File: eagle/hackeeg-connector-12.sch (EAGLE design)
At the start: 21 parts

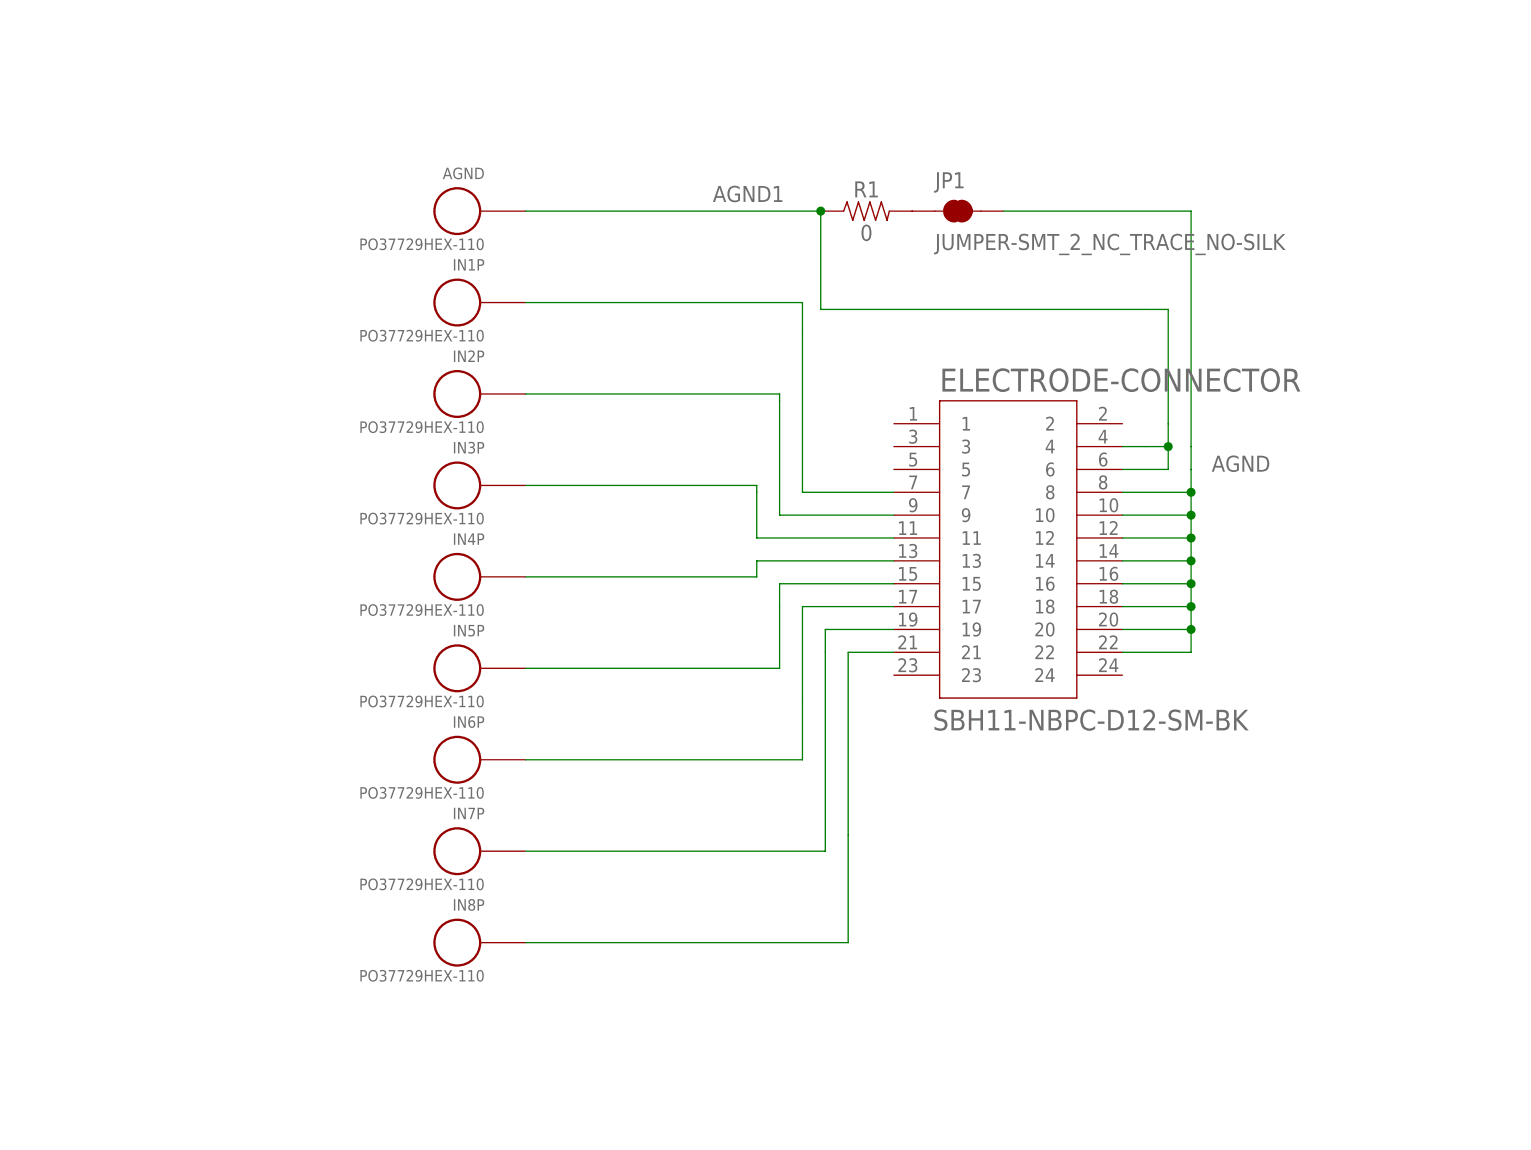
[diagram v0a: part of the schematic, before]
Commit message: added connector, finished schematic and routed
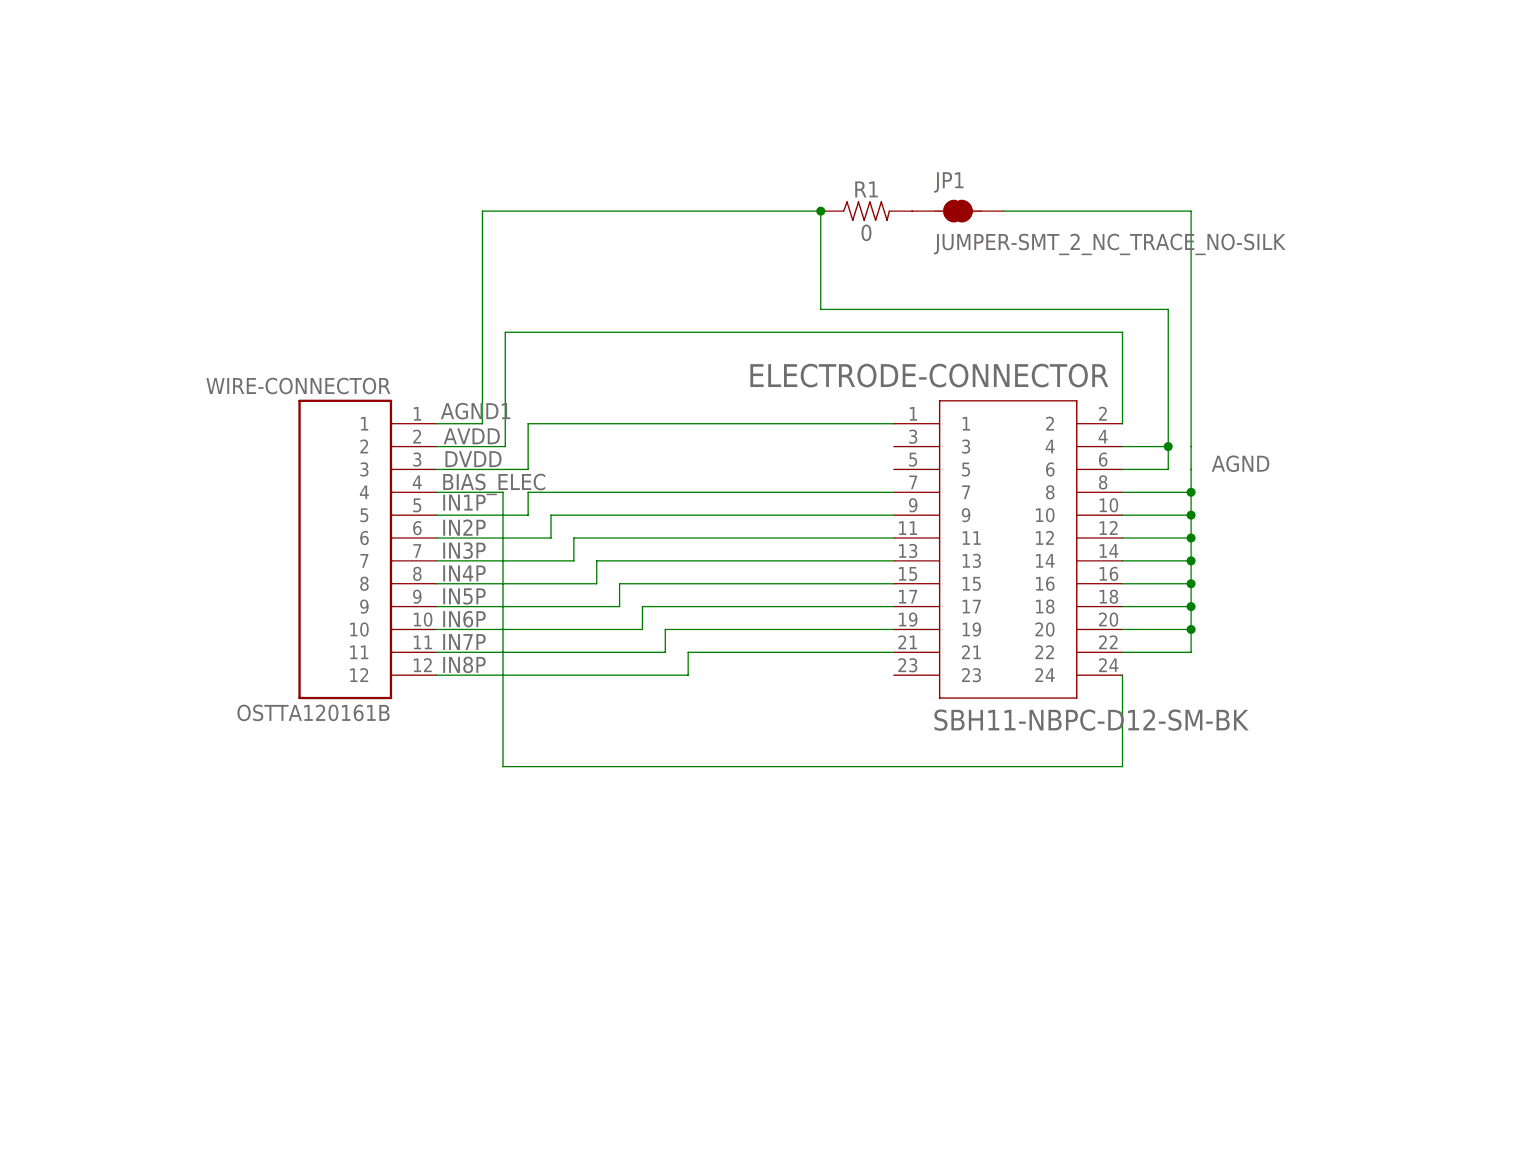
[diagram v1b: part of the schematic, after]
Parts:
- removed AGND, IN1P, IN2P, IN3P, IN4P, IN5P, IN6P, IN7P, IN8P: PO37729HEX-110, po-37729:PO37729HEX-110
- added WIRE-CONNECTOR: OSTTA120161B, OSTTA120161B:OSTTA120161B
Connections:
- removed net N$2: ELECTRODE-CONNECTOR.7, IN1P.SIGNAL
- removed net N$3: ELECTRODE-CONNECTOR.9, IN2P.SIGNAL
- removed net N$4: ELECTRODE-CONNECTOR.11, IN3P.SIGNAL
- removed net N$5: ELECTRODE-CONNECTOR.13, IN4P.SIGNAL
- removed net N$6: ELECTRODE-CONNECTOR.15, IN5P.SIGNAL
- removed net N$7: ELECTRODE-CONNECTOR.17, IN6P.SIGNAL
- removed net N$8: ELECTRODE-CONNECTOR.19, IN7P.SIGNAL
- removed net N$9: ELECTRODE-CONNECTOR.21, IN8P.SIGNAL
- new net AVDD: ELECTRODE-CONNECTOR.2, WIRE-CONNECTOR.2
- new net BIAS_ELEC: ELECTRODE-CONNECTOR.24, WIRE-CONNECTOR.4
- new net DVDD: ELECTRODE-CONNECTOR.1, WIRE-CONNECTOR.3
- new net IN1P: ELECTRODE-CONNECTOR.7, WIRE-CONNECTOR.5
- new net IN2P: ELECTRODE-CONNECTOR.9, WIRE-CONNECTOR.6
- new net IN3P: ELECTRODE-CONNECTOR.11, WIRE-CONNECTOR.7
- new net IN4P: ELECTRODE-CONNECTOR.13, WIRE-CONNECTOR.8
- new net IN5P: ELECTRODE-CONNECTOR.15, WIRE-CONNECTOR.9
- new net IN6P: ELECTRODE-CONNECTOR.17, WIRE-CONNECTOR.10
- new net IN7P: ELECTRODE-CONNECTOR.19, WIRE-CONNECTOR.11
- new net IN8P: ELECTRODE-CONNECTOR.21, WIRE-CONNECTOR.12
- net AGND1: now also WIRE-CONNECTOR.1; no longer AGND.SIGNAL

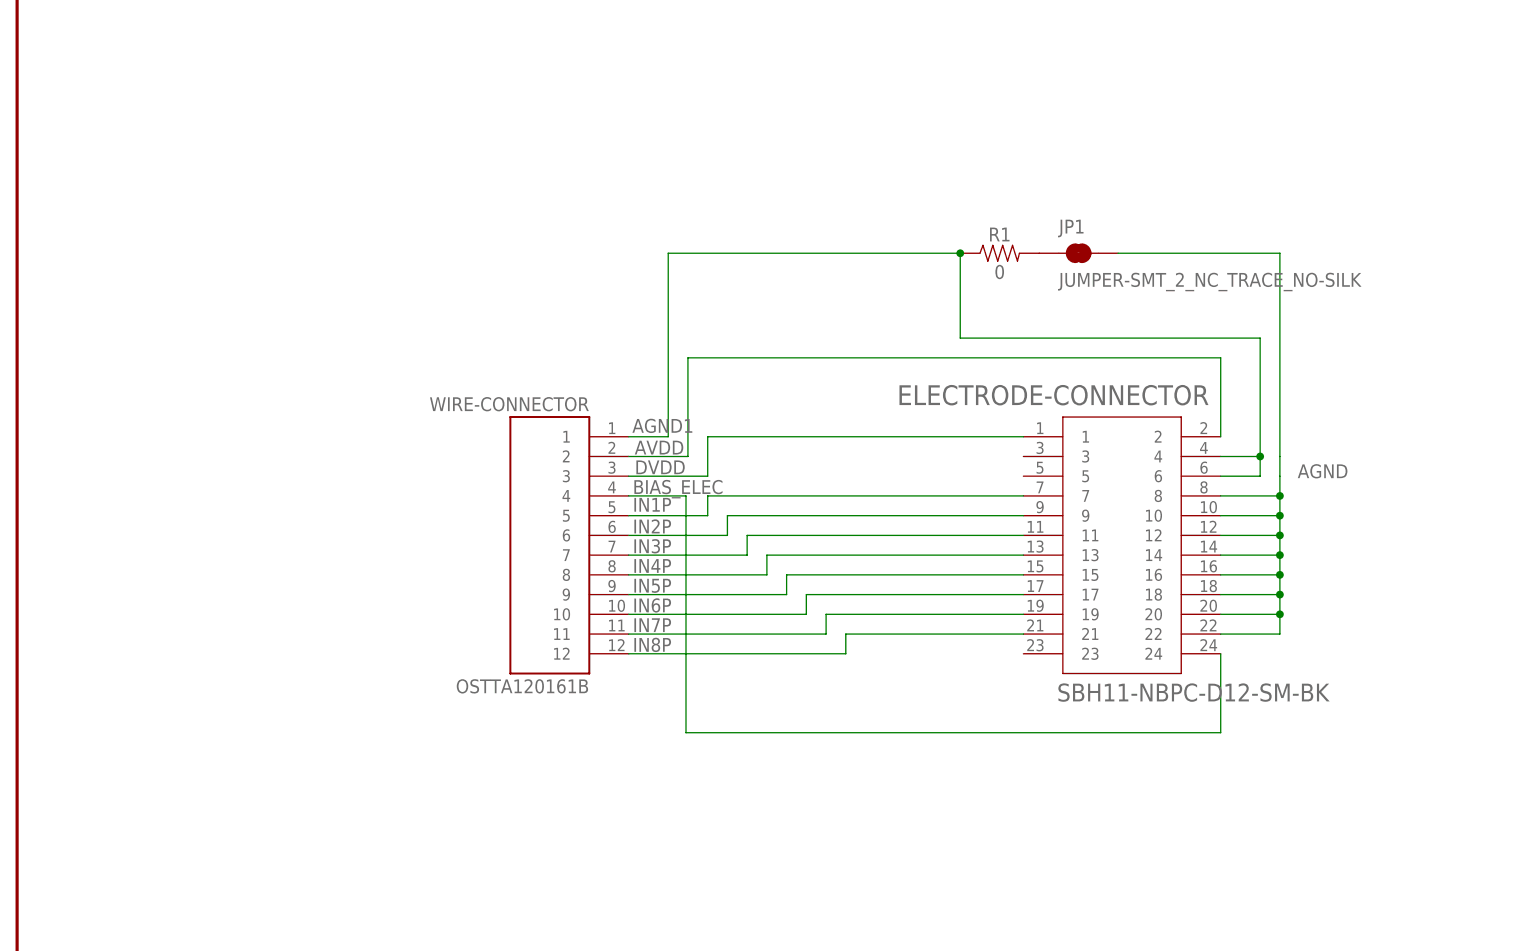
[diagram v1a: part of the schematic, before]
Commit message: put wire connector on bottom of board
- labeled wire connector pins
- board is routed
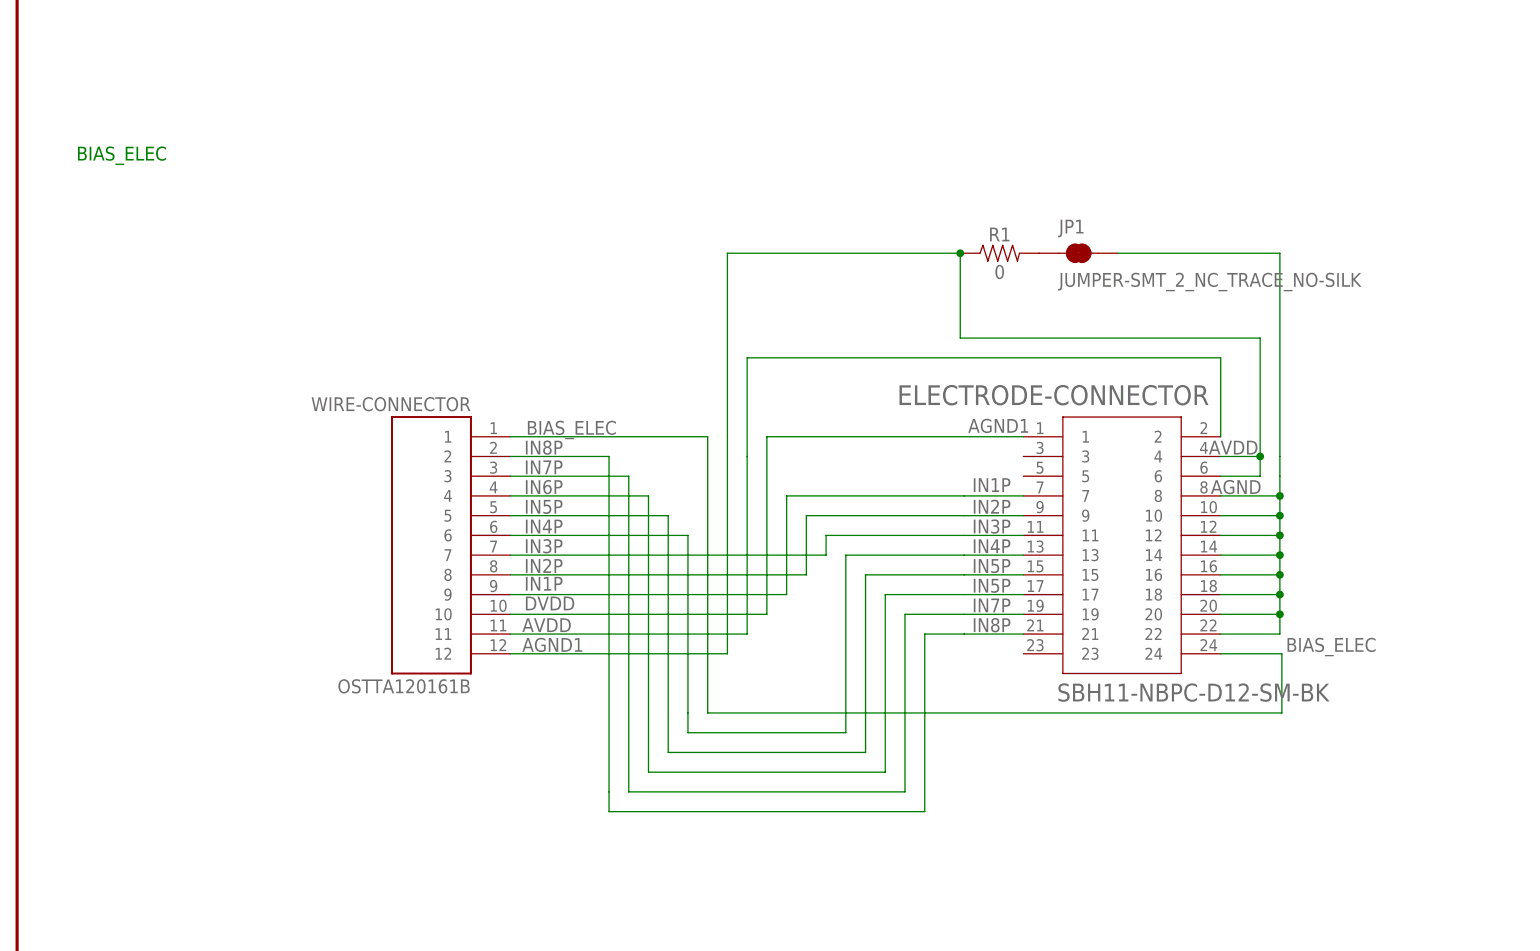
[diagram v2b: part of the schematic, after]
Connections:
- net AGND1: now also WIRE-CONNECTOR.12; no longer WIRE-CONNECTOR.1
- net AVDD: now also WIRE-CONNECTOR.11; no longer WIRE-CONNECTOR.2
- net BIAS_ELEC: now also WIRE-CONNECTOR.1; no longer WIRE-CONNECTOR.4
- net DVDD: now also WIRE-CONNECTOR.10; no longer WIRE-CONNECTOR.3
- net IN1P: now also WIRE-CONNECTOR.9; no longer WIRE-CONNECTOR.5
- net IN2P: now also WIRE-CONNECTOR.8; no longer WIRE-CONNECTOR.6
- net IN4P: now also WIRE-CONNECTOR.6; no longer WIRE-CONNECTOR.8
- net IN5P: now also WIRE-CONNECTOR.5; no longer WIRE-CONNECTOR.9
- net IN6P: now also WIRE-CONNECTOR.4; no longer WIRE-CONNECTOR.10
- net IN7P: now also WIRE-CONNECTOR.3; no longer WIRE-CONNECTOR.11
- net IN8P: now also WIRE-CONNECTOR.2; no longer WIRE-CONNECTOR.12
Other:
- note added: "AGND1"
- note added: "AVDD"
- note added: "BIAS_ELEC"
- note added: "IN1P"
- note added: "IN2P"
- note added: "IN3P"
- note added: "IN4P"
- note added: "IN5P"
- note added: "IN7P"
- note added: "IN8P"
- moved on the sheet: WIRE-CONNECTOR

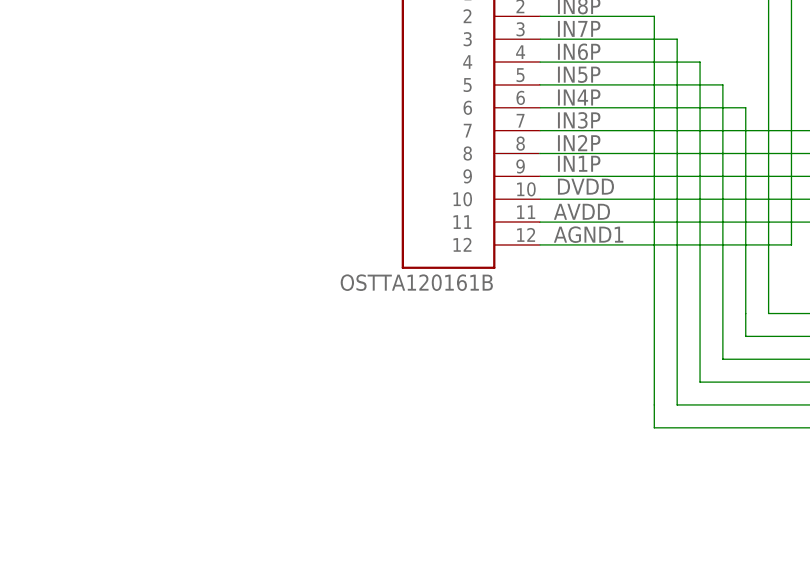
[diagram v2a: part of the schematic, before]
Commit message: replaced OSTTA120161B with OSTTA120161 library
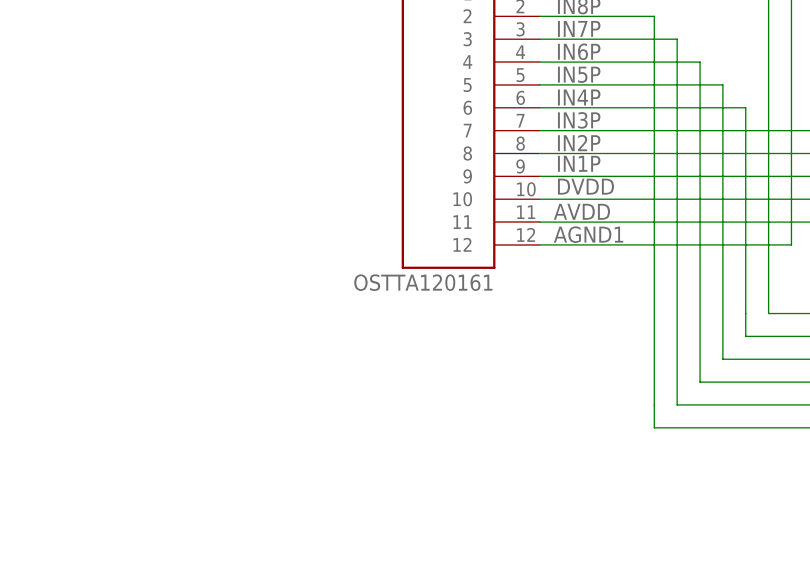
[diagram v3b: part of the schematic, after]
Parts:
- WIRE-CONNECTOR: value OSTTA120161B -> OSTTA120161; device OSTTA120161B:OSTTA120161B -> OSTTA120161:OSTTA120161
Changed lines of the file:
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@@
 <part name="R1" library="SparkFun-Resistors" library_urn="urn:adsk.eagle:library:532" deviceset="0OHM" device="-0603-1/10W-5%" package3d_urn="urn:adsk.eagle:package:39650/1" value="0"/>
 <part name="JP1" library="SparkFun-Jumpers" library_urn="urn:adsk.eagle:library:528" deviceset="JUMPER-SMT_2_NC_TRACE" device="_NO-SILK" package3d_urn="urn:adsk.eagle:package:39286/1"/>
-<part name="WIRE-CONNECTOR" library="OSTTA120161B" deviceset="OSTTA120161B" device=""/>
+<part name="WIRE-CONNECTOR" library="OSTTA120161" deviceset="OSTTA120161" device=""/>
 </parts>
 <sheets>

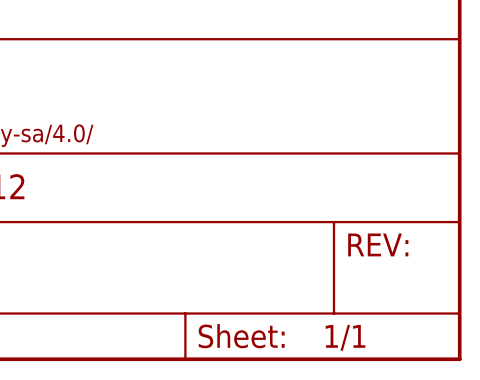
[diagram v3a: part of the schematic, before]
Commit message: add connector version numbers to schematic and PCB
- also added board names to PCBs
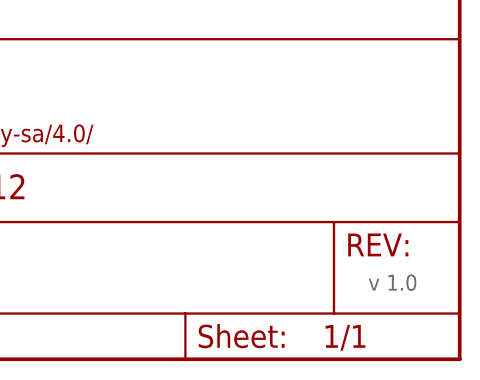
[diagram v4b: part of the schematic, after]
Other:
- note added: "v 1.0"
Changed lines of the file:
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@@
 <?xml version="1.0" encoding="utf-8"?>
 <!DOCTYPE eagle SYSTEM "eagle.dtd">
-<eagle version="9.1.2">
+<eagle version="9.4.0">
 <drawing>
 <settings>
@@
 <text x="272.288" y="168.148" size="1.778" layer="95">AGND1</text>
 <text x="303.276" y="165.354" size="1.778" layer="95">AVDD</text>
+<text x="388.62" y="53.34" size="1.778" layer="95">v 1.0</text>
 </plain>
 <instances>
-<instance part="FRAME1" gate="G$1" x="149.86" y="45.72"/>
-<instance part="FRAME1" gate="V" x="297.18" y="45.72"/>
+<instance part="FRAME1" gate="G$1" x="149.86" y="45.72" smashed="yes"/>
+<instance part="FRAME1" gate="V" x="297.18" y="45.72" smashed="yes">
+<attribute name="LAST_DATE_TIME" x="309.88" y="46.99" size="2.54" layer="94" font="vector"/>
+<attribute name="SHEET" x="383.54" y="46.99" size="2.54" layer="94" font="vector"/>
+<attribute name="DRAWING_NAME" x="312.674" y="63.5" size="2.7432" layer="94" font="vector"/>
+</instance>
 <instance part="ELECTRODE-CONNECTOR" gate="G$1" x="292.1" y="152.4" smashed="yes">
 <attribute name="NAME" x="263.144" y="171.71691875" size="2.54646875" layer="95"/>
 <attribute name="VALUE" x="283.718" y="133.5629" size="2.28846875" layer="96"/>
 </instance>
-<instance part="U$13" gate="G$1" x="193.04" y="53.34"/>
-<instance part="U$1" gate="G$1" x="167.64" y="63.5"/>
-<instance part="FD1" gate="G$1" x="355.6" y="170.18"/>
-<instance part="FD2" gate="G$1" x="355.6" y="182.88"/>
-<instance part="FD3" gate="G$1" x="355.6" y="195.58"/>
-<instance part="FD4" gate="G$1" x="355.6" y="144.78"/>
-<instance part="FD5" gate="G$1" x="355.6" y="132.08"/>
-<instance part="FD6" gate="G$1" x="355.6" y="119.38"/>
-<instance part="R1" gate="G$1" x="276.352" y="191.262"/>
-<instance part="JP1" gate="G$1" x="286.512" y="191.262"/>
-<instance part="WIRE-CONNECTOR" gate="G$1" x="203.2" y="154.94" rot="MR0"/>
+<instance part="U$13" gate="G$1" x="193.04" y="53.34" smashed="yes"/>
+<instance part="U$1" gate="G$1" x="167.64" y="63.5" smashed="yes"/>
+<instance part="FD1" gate="G$1" x="355.6" y="170.18" smashed="yes"/>
+<instance part="FD2" gate="G$1" x="355.6" y="182.88" smashed="yes"/>
+<instance part="FD3" gate="G$1" x="355.6" y="195.58" smashed="yes"/>
+<instance part="FD4" gate="G$1" x="355.6" y="144.78" smashed="yes"/>
+<instance part="FD5" gate="G$1" x="355.6" y="132.08" smashed="yes"/>
+<instance part="FD6" gate="G$1" x="355.6" y="119.38" smashed="yes"/>
+<instance part="R1" gate="G$1" x="276.352" y="191.262" smashed="yes">
+<attribute name="NAME" x="276.352" y="192.786" size="1.778" layer="95" font="vector" align="bottom-center"/>
+<attribute name="VALUE" x="276.352" y="189.738" size="1.778" layer="96" font="vector" align="top-center"/>
+</instance>
+<instance part="JP1" gate="G$1" x="286.512" y="191.262" smashed="yes">
+<attribute name="NAME" x="283.972" y="193.802" size="1.778" layer="95" font="vector"/>
+<attribute name="VALUE" x="283.972" y="188.722" size="1.778" layer="96" font="vector" align="top-left"/>
+</instance>
+<instance part="WIRE-CONNECTOR" gate="G$1" x="203.2" y="154.94" smashed="yes" rot="MR0">
+<attribute name="NAME" x="208.28" y="170.942" size="1.778" layer="95" rot="MR0"/>
+<attribute name="VALUE" x="208.28" y="134.62" size="1.778" layer="96" rot="MR0"/>
+</instance>
 </instances>
 <busses>
